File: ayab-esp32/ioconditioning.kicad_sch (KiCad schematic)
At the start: 43 parts, among them U702 LM393, U703 LM393

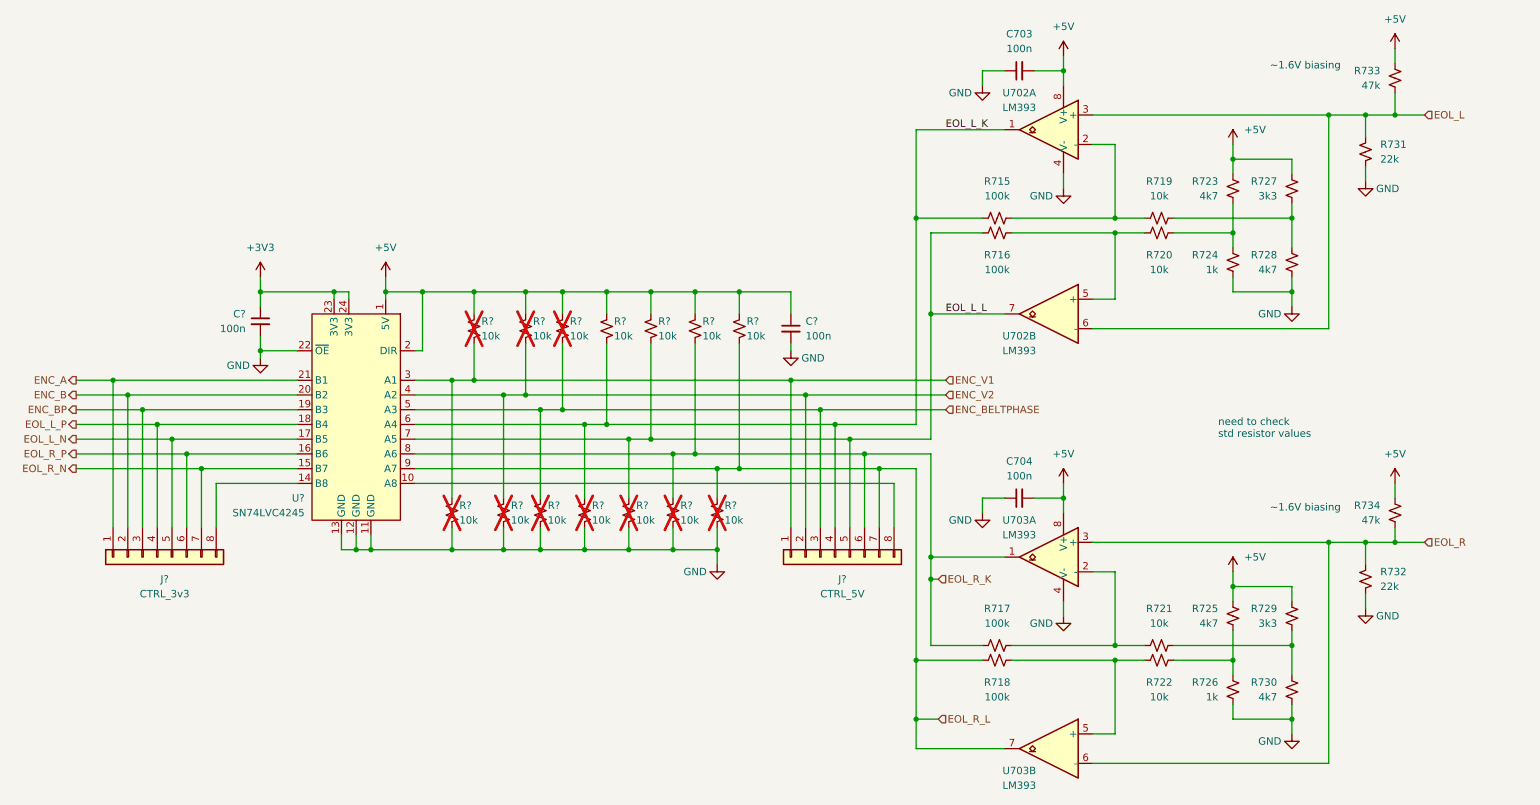
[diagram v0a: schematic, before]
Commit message: work on BOM and parts selection
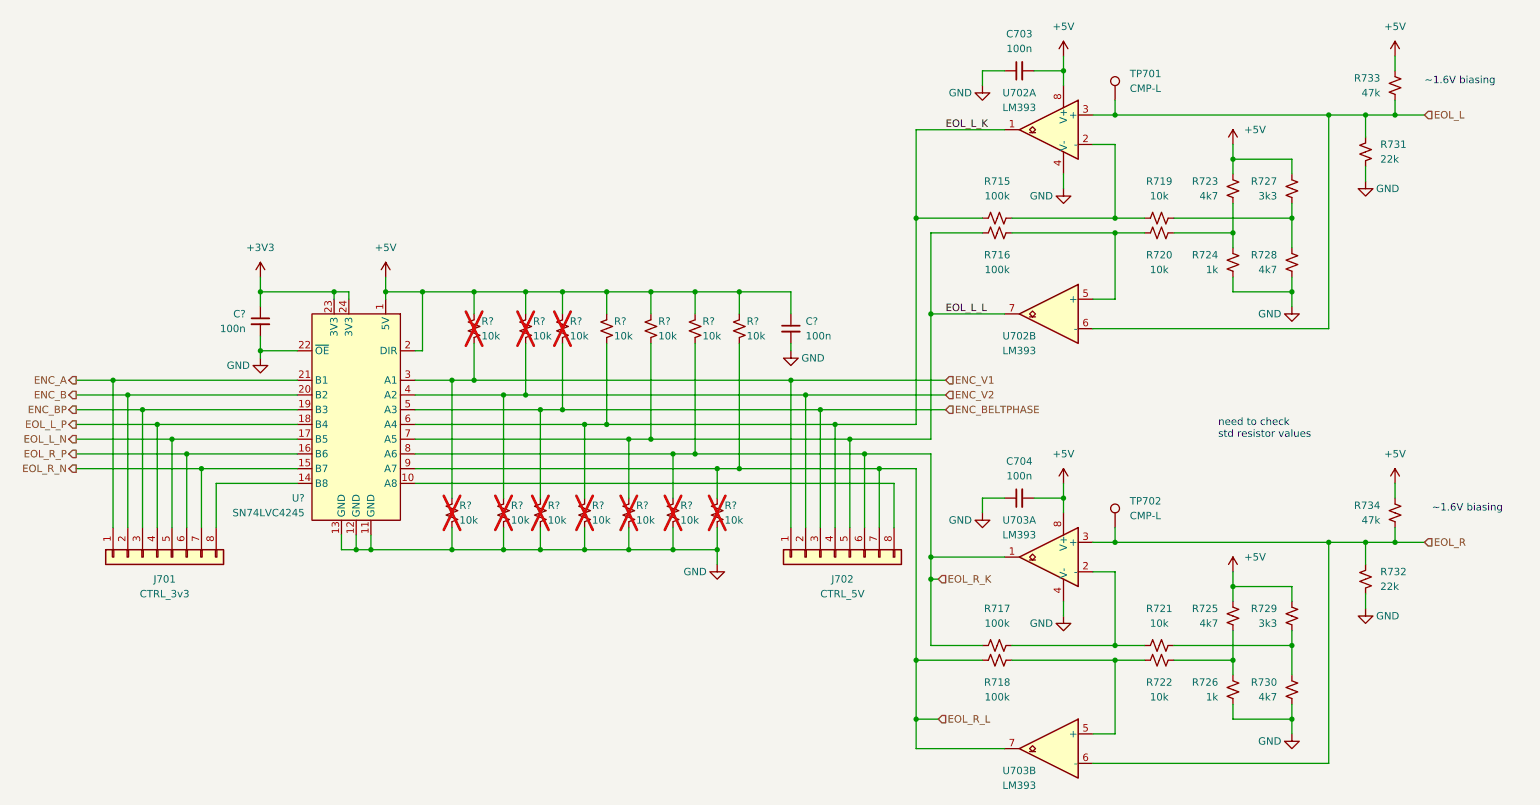
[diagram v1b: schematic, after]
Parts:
- added TP701, TP702: CMP-L, TestPoint:TestPoint_Pad_D2.0mm, symbol Library:TestPoint
- C703, C704, C? (x2): footprint (none) -> Capacitor_SMD:C_0603_1608Metric; symbol ayab-esp32:C_Small -> Library:C_Small; LCSC ID (none) -> C57112; OEM (none) -> FH (Guangdong Fenghua Advanced Tech); OEM PN (none) -> 0603B103K500NT; Package (none) -> 0603; Voltage rating (none) -> 24V X7R
- J701, J702: renamed from J?; footprint (none) -> Connector_PinSocket_2.54mm:PinSocket_2x04_P2.54mm_Vertical; symbol Connector_Generic:Conn_01x08 -> Library:Conn_01x08
- R715, R716, R717, R718: footprint (none) -> Resistor_SMD:R_0603_1608Metric; symbol ayab-esp32:R_Small_US -> Library:R_Small_US; LCSC ID (none) -> C25803; OEM (none) -> UNI-ROYAL(Uniroyal Elec); OEM PN (none) -> 0603WAF1003T5E; Package (none) -> 0603
- R719, R720, R721, R722, R? (x14): footprint (none) -> Resistor_SMD:R_0603_1608Metric; symbol ayab-esp32:R_Small_US -> Library:R_Small_US; LCSC ID (none) -> C25804; OEM (none) -> UNI-ROYAL(Uniroyal Elec); OEM PN (none) -> 0603WAF1002T5E; Package (none) -> 0603
- R723, R725, R728, R730: footprint (none) -> Resistor_SMD:R_0603_1608Metric; symbol ayab-esp32:R_Small_US -> Library:R_Small_US; LCSC ID (none) -> C23162; OEM (none) -> UNI-ROYAL(Uniroyal Elec); OEM PN (none) -> 0603WAF4701T5E; Package (none) -> 0603
- R724, R726: footprint (none) -> Resistor_SMD:R_0603_1608Metric; symbol ayab-esp32:R_Small_US -> Library:R_Small_US; LCSC ID (none) -> C21190; OEM (none) -> UNI-ROYAL(Uniroyal Elec); OEM PN (none) -> 0603WAF1001T5E; Package (none) -> 0603
- R727, R729: footprint (none) -> Resistor_SMD:R_0603_1608Metric; symbol ayab-esp32:R_Small_US -> Library:R_Small_US; LCSC ID (none) -> C22978; OEM (none) -> UNI-ROYAL(Uniroyal Elec); OEM PN (none) -> 0603WAF3301T5E; Package (none) -> 0603
- R731, R732: footprint (none) -> Resistor_SMD:R_0603_1608Metric; symbol ayab-esp32:R_Small_US -> Library:R_Small_US; LCSC ID (none) -> C31850; OEM (none) -> UNI-ROYAL(Uniroyal Elec); OEM PN (none) -> 0603WAF2202T5E; Package (none) -> 0603
- R733, R734: footprint (none) -> Resistor_SMD:R_0603_1608Metric; symbol ayab-esp32:R_Small_US -> Library:R_Small_US; LCSC ID (none) -> C25819; OEM (none) -> UNI-ROYAL(Uniroyal Elec); OEM PN (none) -> 0603WAF4702T5E; Package (none) -> 0603
- U702, U703: footprint (none) -> Package_SO:SOIC-8_3.9x4.9mm_P1.27mm; symbol ayab-esp32:LM393 -> Library:LM393; OEM (none) -> onsemi; OEM PN (none) -> LM393DR2G; Package (none) -> SOIC-8
- U?: symbol ayab-esp32:SN74LVC4245A -> Library:SN74LVC4245A; LCSC ID (none) -> C7859; OEM (none) -> Texas Instruments; OEM PN (none) -> SN74LVC4245APWR; Package (none) -> TSSOP-24
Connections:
- net EOL_L: now also TP701.1
- net EOL_R: now also TP702.1
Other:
- moved on the sheet: R733
